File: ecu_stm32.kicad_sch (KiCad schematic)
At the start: 43 parts, among them J3 ARM Cortex Debug

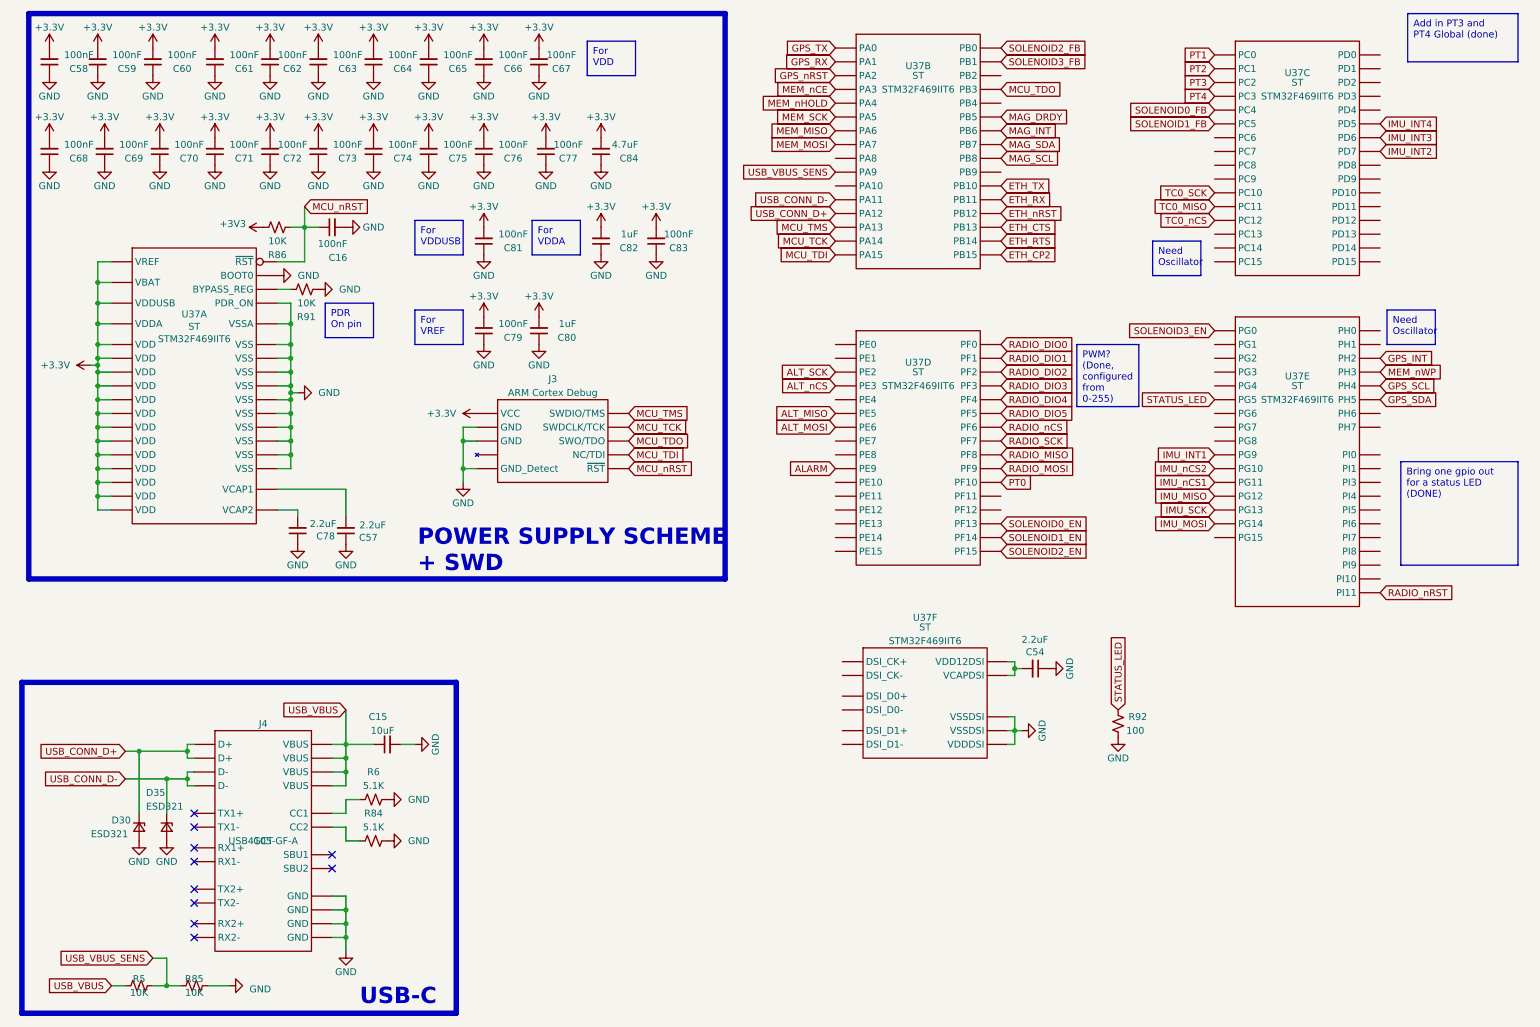
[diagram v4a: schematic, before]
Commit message: added oscillator
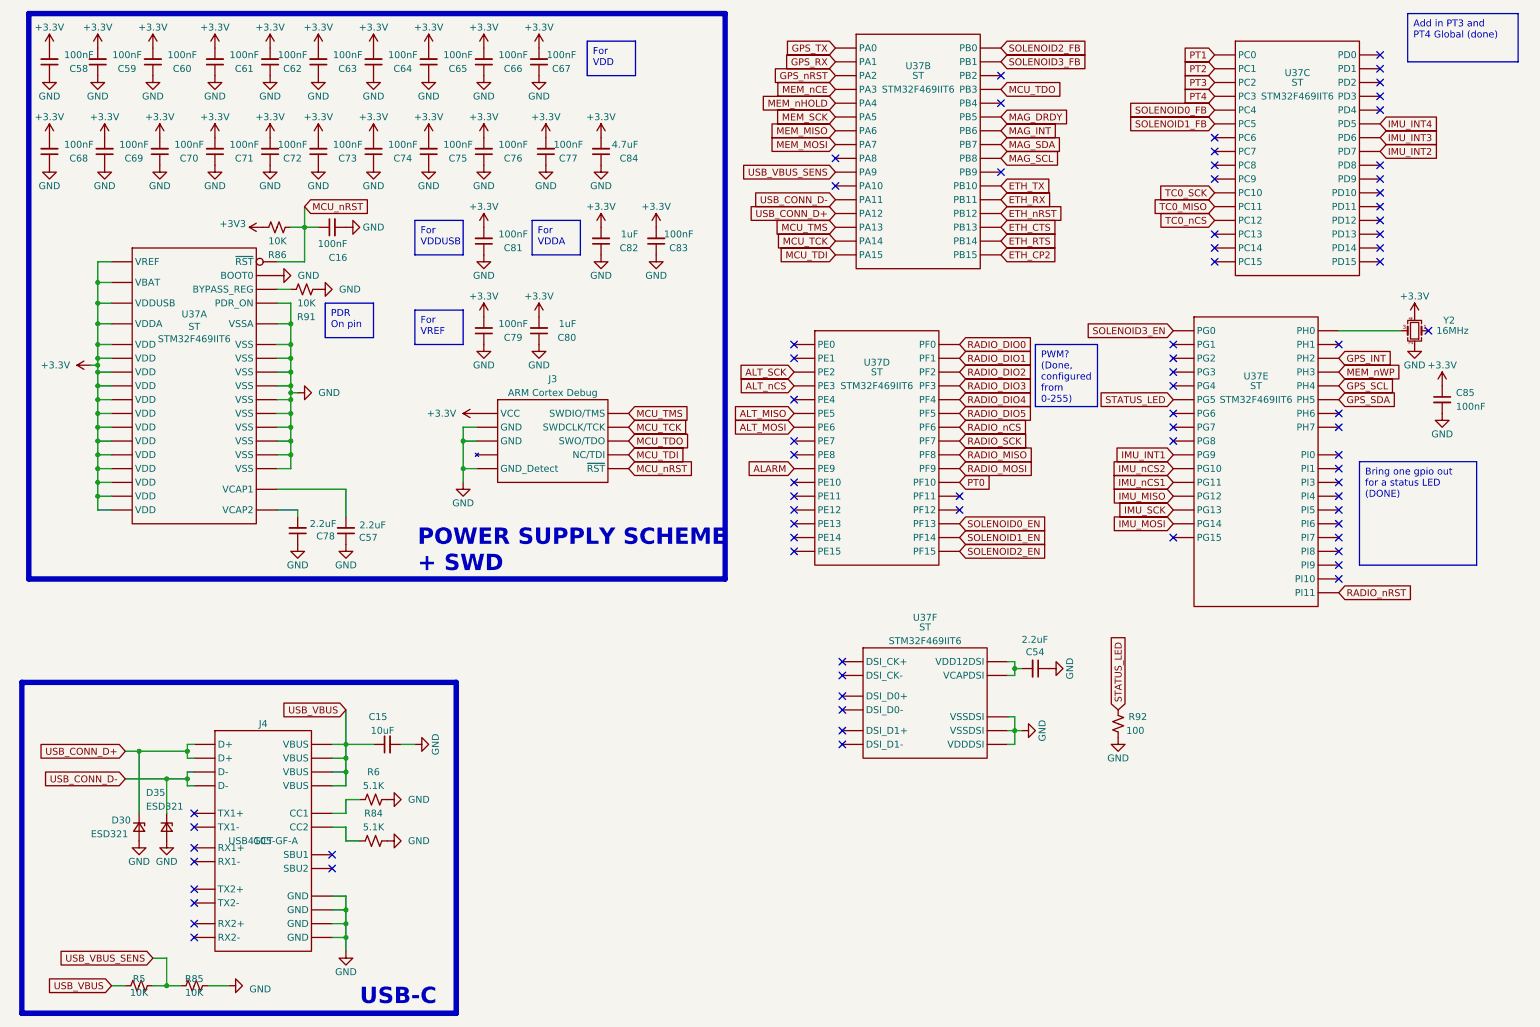
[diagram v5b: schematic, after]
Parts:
- added C85: 100nF, Capacitor_SMD:C_0402_1005Metric, symbol Device:C_Small
- added Y2: 16MHz, Crystal:Crystal_SMD_2016-4Pin_2.0x1.6mm, symbol UCIRP-KiCAD-Lib:Crystal_GND24_Small
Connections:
- net +3.3V: now also C85.1, Y2.4
- net GND: now also C85.2, Y2.2
- net at U37.29 (PH0): now also Y2.3
- no-connect marks 10 -> 76
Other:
- moved on the sheet: U37D, U37E

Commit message: fixed somwe stuff
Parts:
- added D36: LED, LED_SMD:LED_0603_1608Metric_Pad1.05x0.95mm_HandSolder, symbol Device:LED_Small
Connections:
- net GND: now also D36.1 (K); no longer R92.1
- new net: D36.2 (A), R92.1
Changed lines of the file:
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@@
 	(symbol
 		(lib_id "power:GND")
+		(at 214.63 152.4 0)
+		(unit 1)
+		(exclude_from_sim no)
+		(in_bom yes)
+		(on_board yes)
+		(dnp no)
+		(property "Reference" "#PWR0259"
+			(at 214.63 158.75 0)
+			(effects
+				(font
+					(size 1.27 1.27)
+				)
+				(hide yes)
+			)
+		)
+		(property "Value" "GND"
+			(at 214.63 156.21 0)
+			(effects
+				(font
+					(size 1.27 1.27)
+				)
+			)
+		)
+		(property "Footprint" ""
+			(at 214.63 152.4 0)
+			(effects
+				(font
+					(size 1.27 1.27)
+				)
+				(hide yes)
+			)
+		)
+		(property "Datasheet" ""
+			(at 214.63 152.4 0)
+			(effects
+				(font
+					(size 1.27 1.27)
+				)
+				(hide yes)
+			)
+		)
+		(property "Description" ""
+			(at 214.63 152.4 0)
+			(effects
+				(font
+					(size 1.27 1.27)
+				)
+				(hide yes)
+			)
+		)
+		(pin "1"
+		)
+		(instances
+			(project "rocket2-ecu"
+				(path "/02606b2c-b376-4ffb-9781-f9cea3f70994/d71af74c-6b83-4356-8066-aa44d85885b6"
+					(reference "#PWR0259")
+					(unit 1)
+				)
+			)
+		)
+	)
+	(symbol
+		(lib_id "power:GND")
 		(at 269.24 74.93 0)
 		(unit 1)
@@
 	)
 	(symbol
-		(lib_id "power:GND")
-		(at 214.63 147.32 0)
-		(unit 1)
-		(exclude_from_sim no)
-		(in_bom yes)
-		(on_board yes)
-		(dnp no)
-		(property "Reference" "#PWR0259"
-			(at 214.63 153.67 0)
-			(effects
-				(font
-					(size 1.27 1.27)
-				)
-				(hide yes)
-			)
-		)
-		(property "Value" "GND"
-			(at 214.63 151.13 0)
-			(effects
-				(font
-					(size 1.27 1.27)
-				)
-			)
-		)
-		(property "Footprint" ""
-			(at 214.63 147.32 0)
-			(effects
-				(font
-					(size 1.27 1.27)
-				)
-				(hide yes)
-			)
-		)
-		(property "Datasheet" ""
-			(at 214.63 147.32 0)
-			(effects
-				(font
-					(size 1.27 1.27)
-				)
-				(hide yes)
-			)
-		)
-		(property "Description" ""
-			(at 214.63 147.32 0)
-			(effects
-				(font
-					(size 1.27 1.27)
-				)
-				(hide yes)
-			)
-		)
-		(pin "1"
-		)
-		(instances
-			(project "rocket2-ecu"
-				(path "/02606b2c-b376-4ffb-9781-f9cea3f70994/d71af74c-6b83-4356-8066-aa44d85885b6"
-					(reference "#PWR0259")
-					(unit 1)
-				)
-			)
-		)
-	)
-	(symbol
 		(lib_id "Device:D_Zener_Small")
 		(at 39.37 163.83 270)
@@
 					(unit 1)
 				)
+			)
+		)
+	)
+	(symbol
+		(lib_id "Device:LED_Small")
+		(at 214.63 149.86 90)
+		(unit 1)
+		(exclude_from_sim no)
+		(in_bom yes)
+		(on_board yes)
+		(dnp no)
+		(fields_autoplaced yes)
+		(property "Reference" "D36"
+			(at 217.17 148.5264 90)
+			(effects
+				(font
+					(size 1.27 1.27)
+				)
+				(justify right)
+			)
+		)
+		(property "Value" "LED"
+			(at 217.17 151.0664 90)
+			(effects
+				(font
+					(size 1.27 1.27)
+				)
+				(justify right)
+			)
+		)
+		(property "Footprint" "LED_SMD:LED_0603_1608Metric_Pad1.05x0.95mm_HandSolder"
+			(at 214.63 149.86 90)
+			(effects
+				(font
+					(size 1.27 1.27)
+				)
+				(hide yes)
+			)
+		)
+		(property "Datasheet" "~"
+			(at 214.63 149.86 90)
+			(effects
+				(font
+					(size 1.27 1.27)
+				)
+				(hide yes)
+			)
+		)
+		(property "Description" ""
+			(at 214.63 149.86 0)
+			(effects
+				(font
+					(size 1.27 1.27)
+				)
+				(hide yes)
+			)
+		)
+		(property "Manufacturer" "Generic"
+			(at 214.63 149.86 0)
+			(effects
+				(font
+					(size 1.27 1.27)
+				)
+				(hide yes)
+			)
+		)
+		(property "Part #" "Generic 0603 Green LED"
+			(at 214.63 149.86 0)
+			(effects
+				(font
+					(size 1.27 1.27)
+				)
+				(hide yes)
+			)
+		)
+		(pin "1"
+		)
+		(pin "2"
+		)
+		(instances
+			(project "rocket2-ecu"
+				(path "/02606b2c-b376-4ffb-9781-f9cea3f70994/d71af74c-6b83-4356-8066-aa44d85885b6"
+					(reference "D36")
+					(unit 1)
+				)
